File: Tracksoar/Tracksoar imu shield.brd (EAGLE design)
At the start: 44 x 19.5 mm, 12 parts, among them U1 HEX_CONVERTER, U2 LSM9DS1

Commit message: removed old shields
removed square shields and added values to shield passives
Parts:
- C1: value (none) -> 10uf
- C2, C3, C5: value (none) -> .1uf
- C4: value (none) -> 10nf
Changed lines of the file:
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@@
 <attribute name="PROD_ID" value="IC-12536" x="10.0584" y="5.0292" size="1.778" layer="27" rot="R90" display="off"/>
 </element>
-<element name="C1" library="SparkFun-Passives" package="0805" value="" x="16.0274" y="5.2832" rot="R90"/>
-<element name="C2" library="SparkFun-Passives" package="0805" value="" x="13.97" y="5.2578" rot="R90"/>
-<element name="C3" library="SparkFun-Passives" package="0805" value="" x="18.0594" y="5.2832" rot="R90"/>
-<element name="C4" library="SparkFun-Passives" package="0805" value="" x="3.7084" y="4.7752" rot="R180"/>
-<element name="C5" library="SparkFun-Passives" package="0805" value="" x="6.4262" y="4.7752" rot="R90"/>
+<element name="C1" library="SparkFun-Passives" package="0805" value="10uf" x="16.0274" y="5.2832" rot="R90"/>
+<element name="C2" library="SparkFun-Passives" package="0805" value=".1uf" x="13.97" y="5.2578" rot="R90"/>
+<element name="C3" library="SparkFun-Passives" package="0805" value=".1uf" x="18.0594" y="5.2832" rot="R90"/>
+<element name="C4" library="SparkFun-Passives" package="0805" value="10nf" x="3.7084" y="4.7752" rot="R180"/>
+<element name="C5" library="SparkFun-Passives" package="0805" value=".1uf" x="6.4262" y="4.7752" rot="R90"/>
 <element name="U$2" library="SparkFun-PowerIC" package="SOT23-3" value="LM3480IM4" x="17.8308" y="15.1892" rot="MR90"/>
 </elements>

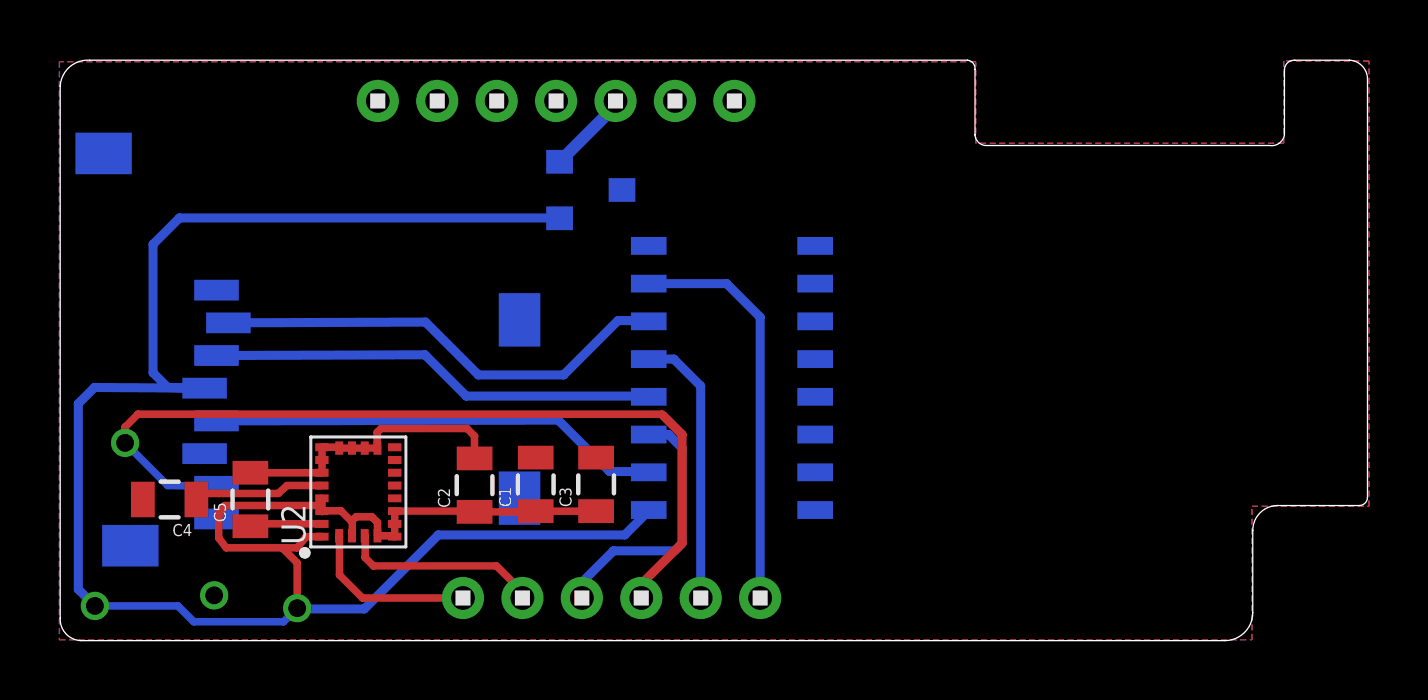
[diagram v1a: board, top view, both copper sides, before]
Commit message: Fixed shield board length
fixed the shield length to not interfere with power and radio
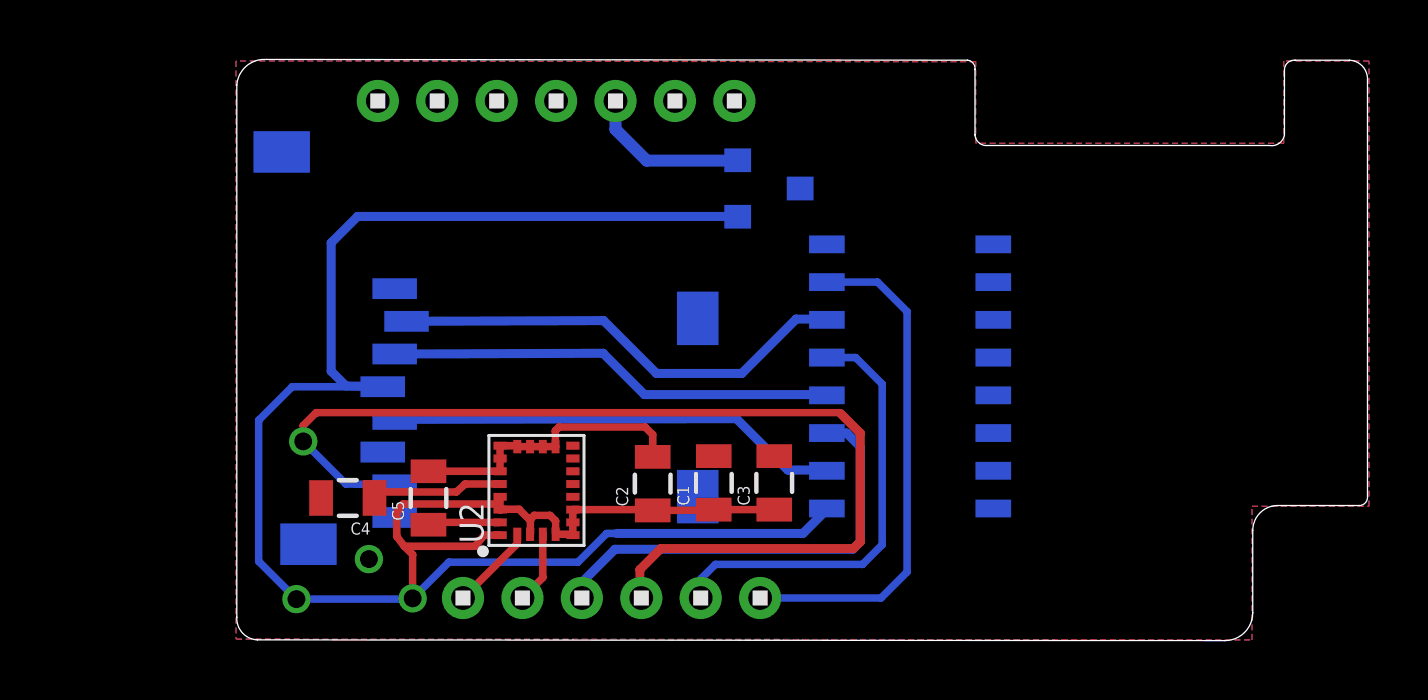
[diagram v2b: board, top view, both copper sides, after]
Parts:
- moved U1 5.99 mm to (28.6, 8.92)
- moved C2 5.99 mm to (20.0, 5.31)
- moved C5 5.99 mm to (12.4, 4.83)
- moved U$1 5.99 mm to (21.9, 2.87)
- moved U2 5.99 mm to (16.1, 5.08)
- moved C4 5.99 mm to (9.70, 4.83)
- moved C1 5.99 mm to (22.0, 5.33)
- moved C3 5.99 mm to (24.1, 5.33)
- moved U$2 5.99 mm to (23.8, 15.2)
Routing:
- net MISO: track 29.5 -> 35.9 mm
- net SCK: track 8.96 -> 15.0 mm
- net MOSI: track 9.26 -> 14.9 mm
- net SDA: track 6.72 -> 2.43 mm
- net SS: track 13.7 -> 17.2 mm
- net SCL: track 5.80 -> 2.90 mm
- net VCC: track 2.83 -> 5.51 mm
- net 3V: track 74.7 -> 72.7 mm
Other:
- board size 44 x 19.5 mm -> 38 x 19.6 mm

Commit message: replaced sd with eeprom
the atmega328p does not have enough SRAM to handle the Trackuino duties
and SD read / write. It has been replace with an ST Micro M24M02 2Mb
eeprom. This will result in much less RAM usage, a smaller BOM, lower
cost, and lower power usage. However it also means we lose portability
of storage and easy computer interfacing. We’ll look at revising this
in future versions.
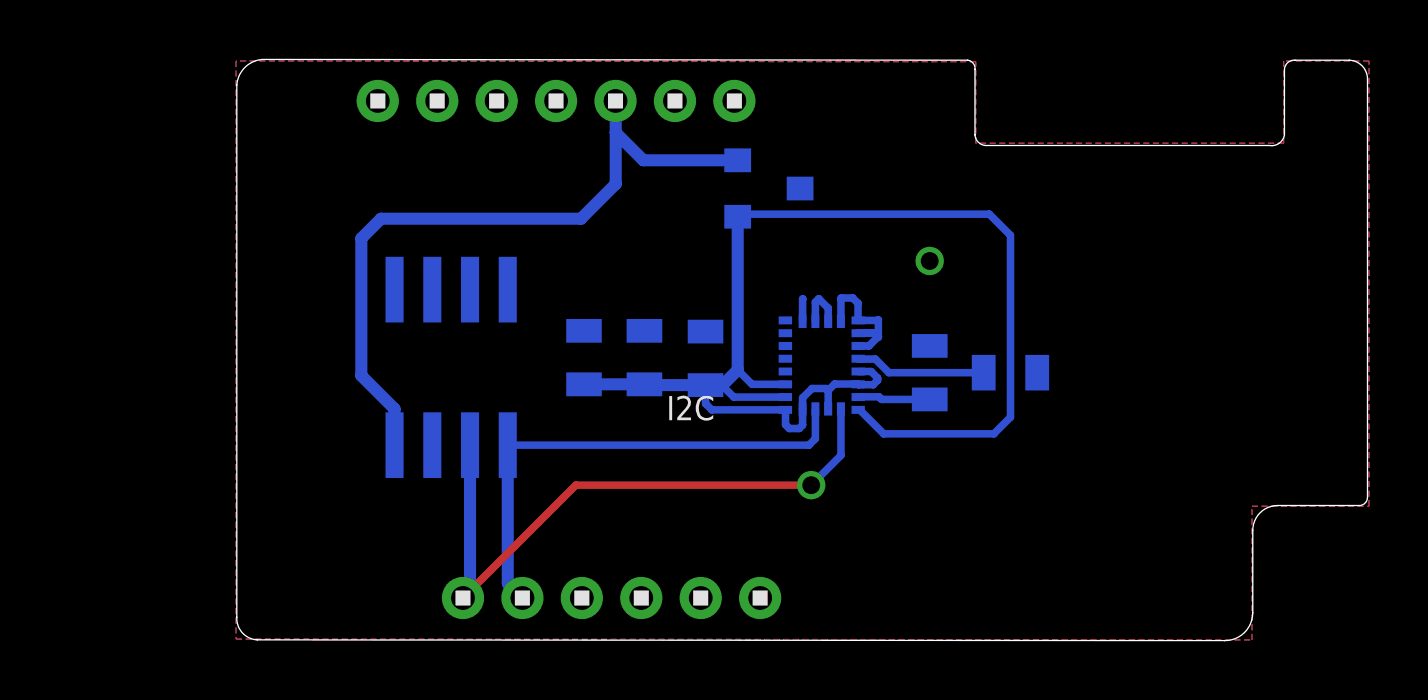
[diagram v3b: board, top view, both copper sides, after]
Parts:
- removed U$1: MICROSD, adafruit:MICROSD
- U1: value HEX_CONVERTER -> EEPROM-I2CSMD; device SparkFun-DigitalIC:SO016 -> SparkFun-DigitalIC:SO08
- moved C4 22.7 mm to (32.0, 9.04), flipped to the bottom
- moved C5 17.4 mm to (29.3, 9.04), flipped to the bottom
- moved U1 15.4 mm to (13.2, 9.22), turned to 180 degrees
- moved U2 10.5 mm to (25.7, 9.30), flipped to the bottom
- moved C3 7.66 mm to (17.7, 9.55), flipped to the bottom
- moved C1 4.82 mm to (19.7, 9.55), flipped to the bottom
- moved C2 4.58 mm to (21.7, 9.53), flipped to the bottom
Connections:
- removed net CS: U$1.2, U1.6
- removed net DI: U$1.3, U1.4
- removed net SCLK: U$1.5, U1.2
- net 3V: no longer U$1.4, U1.1
- net GND: now also U1.4; no longer U$1.6, U$1.MT1, U$1.MT2, U1.11, U1.14, U1.8, U1.9
- net MISO: no longer U$1.7
- net MOSI: no longer U1.5
- net SCK: no longer U1.3
- net SCL: now also U1.6
- net SDA: now also U1.5
- net SS: no longer U1.7
- net VCC: now also U1.8
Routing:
- net MISO: track 35.9 -> 0.00 mm, vias 1 -> 0
- net 3V: track 72.7 -> 45.8 mm, vias 2 -> 0
- net SCL: track 2.90 -> 21.5 mm, vias 0 -> 1
- net VCC: track 5.51 -> 24.0 mm
- net SS: track 17.2 -> 0.00 mm
- net CS: track 15.7 -> 0.00 mm
- net SCLK: track 15.3 -> 0.00 mm
- net DI: track 15.1 -> 0.00 mm
- net SCK: track 15.0 -> 0.00 mm
- net MOSI: track 14.9 -> 0.00 mm
- net SDA: track 2.43 -> 16.8 mm
- net GND: track 9.87 -> 8.01 mm
